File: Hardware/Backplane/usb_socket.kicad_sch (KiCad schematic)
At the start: 7 parts, among them J2102 Molex 105057

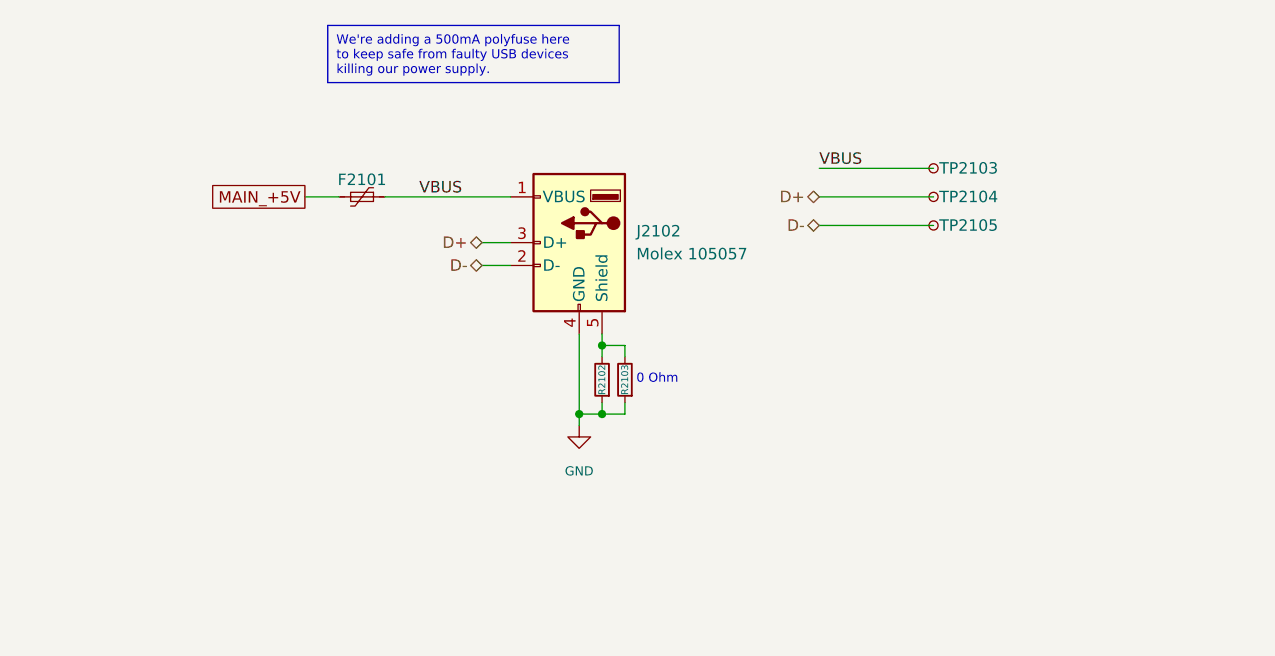
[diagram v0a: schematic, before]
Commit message: Updates the backplane to fit the new platform definition, replaces now deprecated RTC with a new one, improves power management.
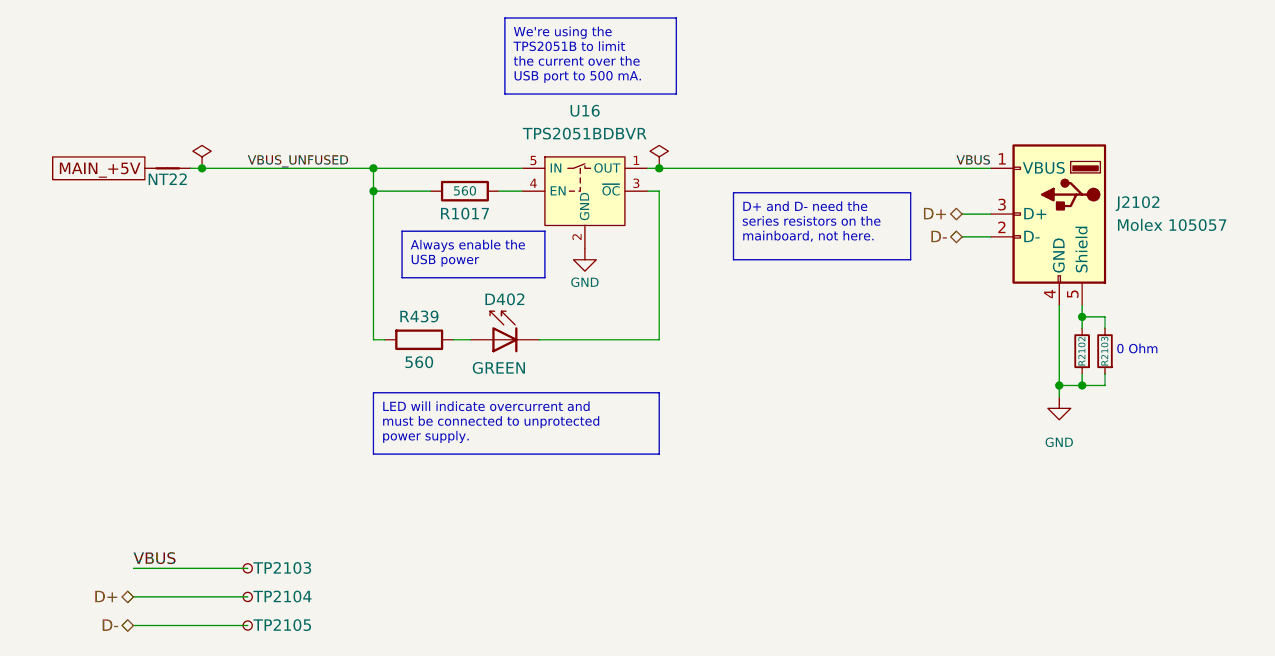
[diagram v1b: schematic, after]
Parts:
- removed F2101: SMD1206B050TF/15, Fuse:Fuse_1206_3216Metric, symbol Symbol Library:SMD1206B050TF/15
- added D402: GREEN, LED_SMD:LED_0603_1608Metric, symbol LED:LD271
- added NT22: NetTie_2, NetTie:NetTie-2_SMD_Pad0.5mm, symbol Device:NetTie_2
- added R1017, R439: 560, Resistor_SMD:R_0603_1608Metric, symbol Device:R
- added U16: TPS2051BDBVR, Package_TO_SOT_SMD:SOT-23-5, symbol Home Computer:TPS2051BDBVR
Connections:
- net GND: now also U16.2 (GND)
- net MAIN_+5V: now also NT22.1
- net VBUS: now also U16.1 (OUT)
- new net: D402.2 (A), R439.1
- new net: D402.1 (K), U16.3 (~{OC})
- new net: R1017.1, U16.4 (EN)
- new net VBUS_UNFUSED: NT22.2, R1017.2, R439.2, U16.5 (IN)
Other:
- moved on the sheet: J2102, R2102, R2103, TP2103, TP2104, TP2105

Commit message: Improves backplane schematic even more
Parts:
- added C132: 100n, Capacitor_SMD:C_0603_1608Metric, symbol Device:C
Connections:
- net GND: now also C132.1
- net VBUS_UNFUSED: now also C132.2
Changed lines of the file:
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@@
-	)
-	(junction
-		(at 90.17 50.8)
-		(diameter 0)
-		(color 0 0 0 0)
 	)
 	(junction
@@
 	)
 	(junction
+		(at 50.8 50.8)
+		(diameter 0)
+		(color 0 0 0 0)
+	)
+	(junction
 		(at 58.42 53.34)
 		(diameter 0)
@@
 	(wire
 		(pts
-			(xy 90.17 50.8) (xy 127 50.8)
+			(xy 50.8 69.85) (xy 50.8 64.135)
+		)
+		(stroke
+			(width 0)
+			(type default)
+		)
+	)
+	(wire
+		(pts
+			(xy 88.9 50.8) (xy 127 50.8)
 		)
 		(stroke
@@
 	(wire
 		(pts
-			(xy 39.37 50.8) (xy 74.93 50.8)
+			(xy 39.37 50.8) (xy 50.8 50.8)
 		)
 		(stroke
@@
 	(wire
 		(pts
-			(xy 88.9 50.8) (xy 90.17 50.8)
-		)
-		(stroke
-			(width 0)
-			(type default)
-		)
-	)
-	(wire
-		(pts
 			(xy 76.835 69.85) (xy 90.17 69.85)
 		)
@@
 	(wire
 		(pts
+			(xy 50.8 50.8) (xy 50.8 56.515)
+		)
+		(stroke
+			(width 0)
+			(type default)
+		)
+	)
+	(wire
+		(pts
 			(xy 139.7 73.66) (xy 139.7 74.93)
 		)
@@
 		(pts
 			(xy 58.42 53.34) (xy 58.42 69.85)
+		)
+		(stroke
+			(width 0)
+			(type default)
+		)
+	)
+	(wire
+		(pts
+			(xy 50.8 50.8) (xy 74.93 50.8)
 		)
 		(stroke
@@
 	)
 	(symbol
-		(lib_id "power:PWR_FLAG")
-		(at 90.17 50.8 0)
-		(mirror y)
-		(unit 1)
-		(body_style 1)
-		(exclude_from_sim no)
-		(in_bom yes)
-		(on_board yes)
-		(in_pos_files yes)
-		(dnp no)
-		(fields_autoplaced yes)
-		(property "Reference" "#FLG0439"
-			(at 90.17 48.895 0)
-			(hide yes)
-			(show_name no)
-			(do_not_autoplace no)
-			(effects
-				(font
-					(size 1.016 1.016)
-				)
-			)
-		)
-		(property "Value" "PWR_FLAG"
-			(at 90.17 45.72 0)
-			(hide yes)
-			(show_name no)
-			(do_not_autoplace no)
-			(effects
-				(font
-					(size 1.016 1.016)
-				)
-			)
-		)
-		(property "Footprint" ""
-			(at 90.17 50.8 0)
-			(hide yes)
-			(show_name no)
-			(do_not_autoplace no)
-			(effects
-				(font
-					(size 1.27 1.27)
-				)
-			)
-		)
-		(property "Datasheet" ""
-			(at 90.17 50.8 0)
-			(hide yes)
-			(show_name no)
-			(do_not_autoplace no)
-			(effects
-				(font
-					(size 1.27 1.27)
-				)
-			)
-		)
-		(property "Description" "Special symbol for telling ERC where power comes from"
-			(at 90.17 50.8 0)
-			(hide yes)
-			(show_name no)
-			(do_not_autoplace no)
-			(effects
-				(font
-					(size 1.27 1.27)
-				)
-			)
-		)
-		(pin "1"
-		)
-		(instances
-			(project "Backplane"
-				(path "/c6da991a-d3ed-4ac1-8b0d-12cd7ba8539b/d722aa70-6517-4527-99e3-acc9d055bb81"
-					(reference "#FLG0440")
-					(unit 1)
-				)
-				(path "/c6da991a-d3ed-4ac1-8b0d-12cd7ba8539b/fc1f9b60-4d70-43c3-b323-949d6cdfaf31"
-					(reference "#FLG0439")
-					(unit 1)
-				)
-			)
-		)
-	)
-	(symbol
 		(lib_id "Device:NetTie_2")
 		(at 35.56 50.8 0)
@@
 				(path "/c6da991a-d3ed-4ac1-8b0d-12cd7ba8539b/fc1f9b60-4d70-43c3-b323-949d6cdfaf31"
 					(reference "TP2104")
+					(unit 1)
+				)
+			)
+		)
+	)
+	(symbol
+		(lib_id "Device:C")
+		(at 50.8 60.325 0)
+		(mirror x)
+		(unit 1)
+		(body_style 1)
+		(exclude_from_sim no)
+		(in_bom yes)
+		(on_board yes)
+		(in_pos_files yes)
+		(dnp no)
+		(property "Reference" "C132"
+			(at 47.625 59.0549 0)
+			(show_name no)
+			(do_not_autoplace no)
+			(effects
+				(font
+					(size 1.016 1.016)
+				)
+				(justify right)
+			)
+		)
+		(property "Value" "100n"
+			(at 47.625 61.5949 0)
+			(show_name no)
+			(do_not_autoplace no)
+			(effects
+				(font
+					(size 1.016 1.016)
+				)
+				(justify right)
+			)
+		)
+		(property "Footprint" "Capacitor_SMD:C_0603_1608Metric"
+			(at 51.7652 56.515 0)
+			(hide yes)
+			(show_name no)
+			(do_not_autoplace no)
+			(effects
+				(font
+					(size 1.27 1.27)
+				)
+			)
+		)
+		(property "Datasheet" "https://www.yageogroup.com/content/datasheet/asset/file/KEM_C1002_X7R_SMD"
+			(at 50.8 60.325 0)
+			(hide yes)
+			(show_name no)
+			(do_not_autoplace no)
+			(effects
+				(font
+					(size 1.27 1.27)
+				)
+			)
+		)
+		(property "Description" "Unpolarized capacitor"
+			(at 50.8 60.325 0)
+			(hide yes)
+			(show_name no)
+			(do_not_autoplace no)
+			(effects
+				(font
+					(size 1.27 1.27)
+				)
+			)
+		)
+		(property "Digikey Part No" "399-C0603C104M4RACTUCT-ND"
+			(at 50.8 60.325 0)
+			(hide yes)
+			(show_name no)
+			(do_not_autoplace no)
+			(effects
+				(font
+					(size 1.27 1.27)
+				)
+			)
+		)
+		(pin "2"
+		)
+		(pin "1"
+		)
+		(instances
+			(project "Backplane"
+				(path "/c6da991a-d3ed-4ac1-8b0d-12cd7ba8539b/d722aa70-6517-4527-99e3-acc9d055bb81"
+					(reference "C133")
+					(unit 1)
+				)
+				(path "/c6da991a-d3ed-4ac1-8b0d-12cd7ba8539b/fc1f9b60-4d70-43c3-b323-949d6cdfaf31"
+					(reference "C132")
 					(unit 1)
 				)
@@
 					(unit 1)
 				)
+			)
+		)
+	)
+	(symbol
+		(lib_id "power:GND")
+		(at 50.8 69.85 0)
+		(unit 1)
+		(body_style 1)
+		(exclude_from_sim no)
+		(in_bom yes)
+		(on_board yes)
+		(in_pos_files yes)
+		(dnp no)
+		(property "Reference" "#PWR0166"
+			(at 50.8 76.2 0)
+			(hide yes)
+			(show_name no)
+			(do_not_autoplace no)
+			(effects
+				(font
+					(size 1.016 1.016)
+				)
+			)
+		)
+		(property "Value" "GND"
+			(at 50.8 73.025 0)
+			(show_name no)
+			(do_not_autoplace no)
+			(effects
+				(font
+					(size 1.016 1.016)
+				)
+				(justify top)
+			)
+		)
+		(property "Footprint" ""
+			(at 50.8 69.85 0)
+			(hide yes)
+			(show_name no)
+			(do_not_autoplace no)
+			(effects
+				(font
+					(size 1.27 1.27)
+				)
+			)
+		)
+		(property "Datasheet" ""
+			(at 50.8 69.85 0)
+			(hide yes)
+			(show_name no)
+			(do_not_autoplace no)
+			(effects
+				(font
+					(size 1.27 1.27)
+				)
+			)
+		)
+		(property "Description" "Power symbol creates a global label with name \"GND\" , ground"
+			(at 50.8 69.85 0)
+			(hide yes)
+			(show_name no)
+			(do_not_autoplace no)
+			(effects
+				(font
+					(size 1.27 1.27)
+				)
+			)
+		)
+		(pin "1"
+		)
+		(instances
+			(project "Backplane"
+				(path "/c6da991a-d3ed-4ac1-8b0d-12cd7ba8539b/d722aa70-6517-4527-99e3-acc9d055bb81"
+					(reference "#PWR0167")
+					(unit 1)
+				)
+				(path "/c6da991a-d3ed-4ac1-8b0d-12cd7ba8539b/fc1f9b60-4d70-43c3-b323-949d6cdfaf31"
+					(reference "#PWR0166")
+					(unit 1)
+				)
